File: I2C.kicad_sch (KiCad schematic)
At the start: 14 parts, among them J701 Conn_01x04, J702 Conn_01x04, U701 RCLAMP0524P-N

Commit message: Rename Ferrite_Bead to FerriteBead
Symbol name changed between KiCad 5 and 6...
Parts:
- FB701, FB702, FB703: symbol Device:Ferrite_Bead -> Device:FerriteBead
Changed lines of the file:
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@@
     (pin "1")
   )
-  (symbol (lib_id "Device:Ferrite_Bead") (at 142.24 68.58 90) (mirror x) (unit 1)
+  (symbol (lib_id "Device:FerriteBead") (at 142.24 68.58 90) (mirror x) (unit 1)
     (in_bom yes) (on_board yes)
     (property "Reference" "FB701" (id 0) (at 142.24 61.6204 90))
@@
     (pin "2")
   )
-  (symbol (lib_id "Device:Ferrite_Bead") (at 142.24 109.22 90) (mirror x) (unit 1)
+  (symbol (lib_id "Device:FerriteBead") (at 142.24 109.22 90) (mirror x) (unit 1)
     (in_bom yes) (on_board yes)
     (property "Reference" "FB703" (id 0) (at 142.24 102.2604 90))
@@
     (pin "2")
   )
-  (symbol (lib_id "Device:Ferrite_Bead") (at 142.24 88.9 90) (mirror x) (unit 1)
+  (symbol (lib_id "Device:FerriteBead") (at 142.24 88.9 90) (mirror x) (unit 1)
     (in_bom yes) (on_board yes)
     (property "Reference" "FB702" (id 0) (at 142.24 81.9404 90))

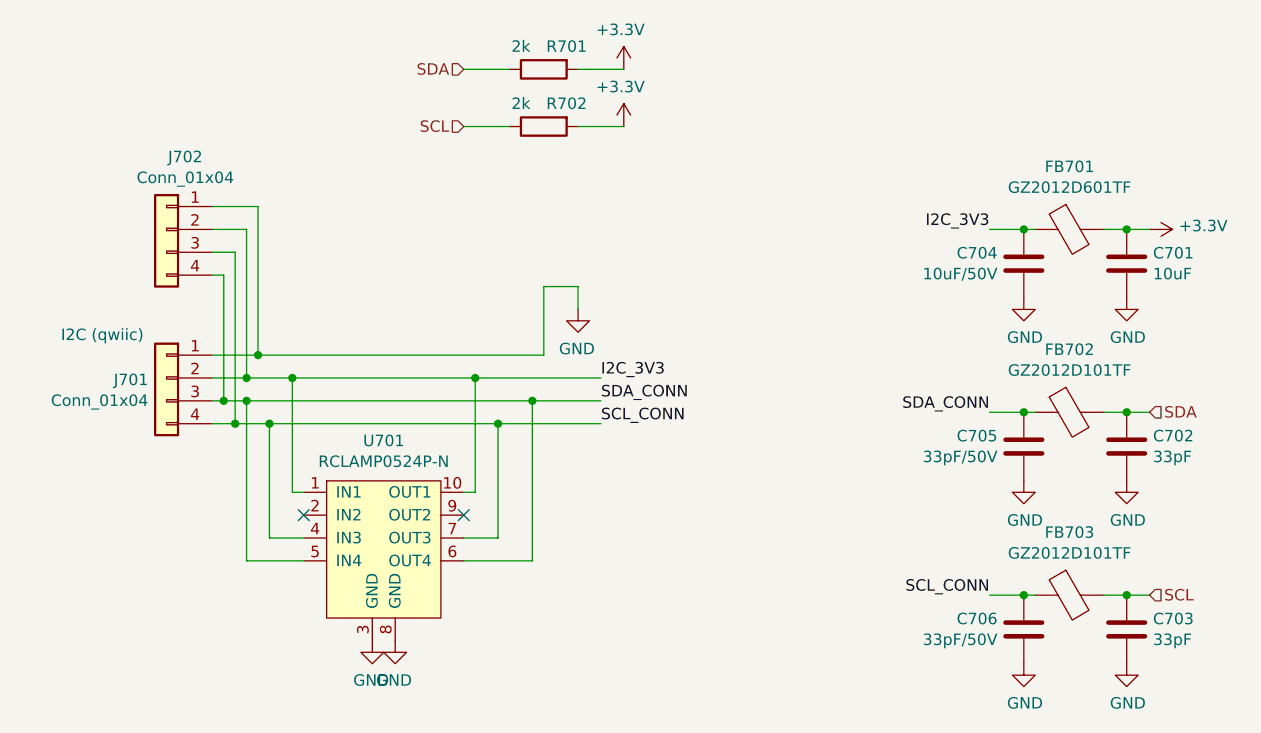
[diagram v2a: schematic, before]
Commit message: Only use the edge signal pins of RCLAMPs if possible
This improves resiliency to slight misalignment during manufacturing.
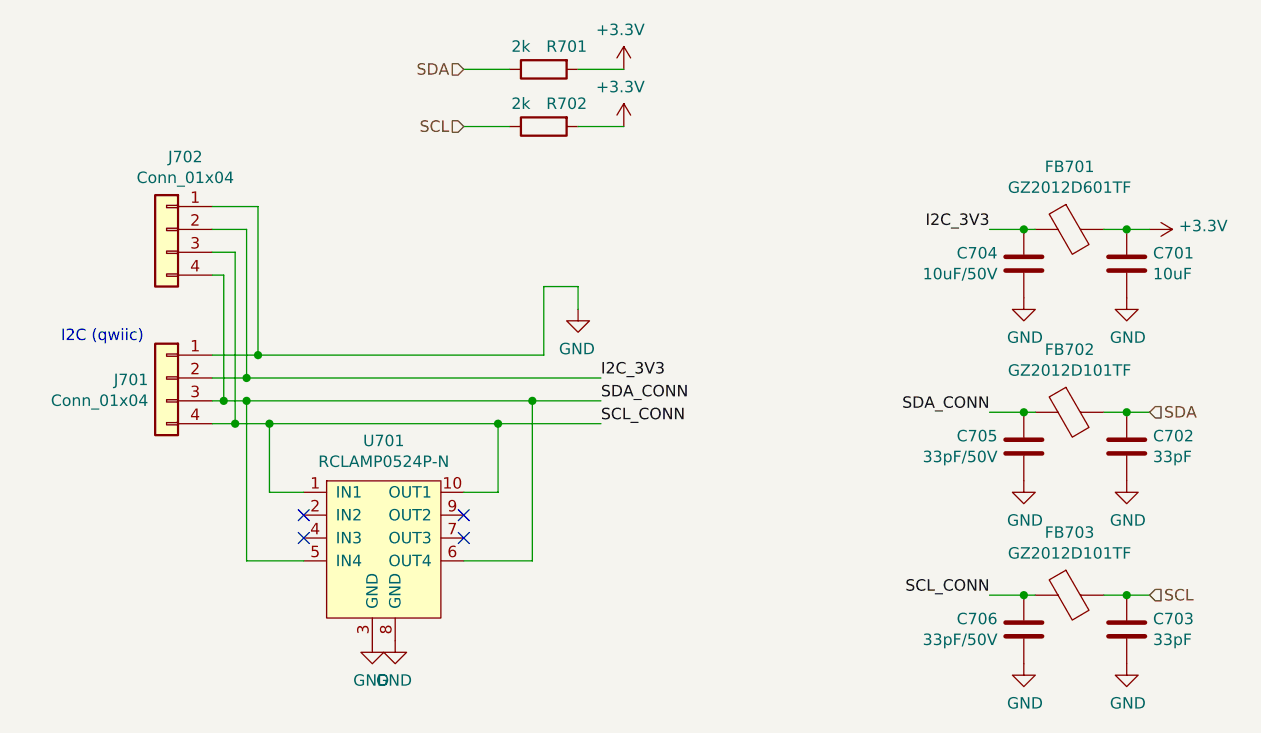
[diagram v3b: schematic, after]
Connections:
- net I2C_3V3: no longer U701.1 (IN1), U701.10 (OUT1)
- net SCL_CONN: now also U701.1 (IN1), U701.10 (OUT1); no longer U701.4 (IN3), U701.7 (OUT3)
- no-connect marks 2 -> 4
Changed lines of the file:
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@@
     (comment 3 "SH-ESP32 is licensed under CC BY-SA 4.0.")
-  )
-  (junction (at 55.88 85.09) (diameter 0) (color 0 0 0 0)
   )
   (junction (at 137.16 109.22) (diameter 0) (color 0 0 0 0)
@@
   (junction (at 50.8 87.63) (diameter 0) (color 0 0 0 0)
   )
-  (junction (at 76.2 85.09) (diameter 0) (color 0 0 0 0)
-  )
+  (no_connect (at 74.93 102.87))
   (no_connect (at 57.15 100.33))
   (no_connect (at 74.93 100.33))
+  (no_connect (at 57.15 102.87))
   (wire (pts (xy 52.07 66.04) (xy 52.07 82.55))
     (stroke (width 0) (type default) (color 0 0 0 0))
@@
   )
   (wire (pts (xy 50.8 105.41) (xy 50.8 87.63))
-    (stroke (width 0) (type default) (color 0 0 0 0))
-  )
-  (wire (pts (xy 55.88 85.09) (xy 50.8 85.09))
     (stroke (width 0) (type default) (color 0 0 0 0))
   )
@@
     (stroke (width 0) (type default) (color 0 0 0 0))
   )
-  (wire (pts (xy 55.88 97.79) (xy 55.88 85.09))
-    (stroke (width 0) (type default) (color 0 0 0 0))
-  )
   (wire (pts (xy 74.93 50.8) (xy 80.01 50.8))
     (stroke (width 0) (type default) (color 0 0 0 0))
@@
     (stroke (width 0) (type default) (color 0 0 0 0))
   )
-  (wire (pts (xy 74.93 97.79) (xy 76.2 97.79))
+  (wire (pts (xy 74.93 97.79) (xy 78.74 97.79))
     (stroke (width 0) (type default) (color 0 0 0 0))
   )
@@
     (stroke (width 0) (type default) (color 0 0 0 0))
   )
-  (wire (pts (xy 76.2 85.09) (xy 55.88 85.09))
+  (wire (pts (xy 50.8 85.09) (xy 90.17 85.09))
     (stroke (width 0) (type default) (color 0 0 0 0))
   )
@@
     (stroke (width 0) (type default) (color 0 0 0 0))
   )
-  (wire (pts (xy 76.2 97.79) (xy 76.2 85.09))
-    (stroke (width 0) (type default) (color 0 0 0 0))
-  )
   (wire (pts (xy 83.82 74.93) (xy 87.63 74.93))
     (stroke (width 0) (type default) (color 0 0 0 0))
@@
     (stroke (width 0) (type default) (color 0 0 0 0))
   )
-  (wire (pts (xy 53.34 102.87) (xy 53.34 90.17))
+  (wire (pts (xy 53.34 97.79) (xy 53.34 90.17))
     (stroke (width 0) (type default) (color 0 0 0 0))
   )
@@
     (stroke (width 0) (type default) (color 0 0 0 0))
   )
-  (wire (pts (xy 78.74 90.17) (xy 78.74 102.87))
+  (wire (pts (xy 78.74 90.17) (xy 78.74 97.79))
     (stroke (width 0) (type default) (color 0 0 0 0))
   )
   (wire (pts (xy 49.53 71.12) (xy 49.53 90.17))
-    (stroke (width 0) (type default) (color 0 0 0 0))
-  )
-  (wire (pts (xy 90.17 85.09) (xy 76.2 85.09))
     (stroke (width 0) (type default) (color 0 0 0 0))
   )
@@
     (stroke (width 0) (type default) (color 0 0 0 0))
   )
-  (wire (pts (xy 46.99 66.04) (xy 52.07 66.04))
+  (wire (pts (xy 53.34 97.79) (xy 57.15 97.79))
     (stroke (width 0) (type default) (color 0 0 0 0))
   )
-  (wire (pts (xy 57.15 102.87) (xy 53.34 102.87))
-    (stroke (width 0) (type default) (color 0 0 0 0))
-  )
-  (wire (pts (xy 57.15 97.79) (xy 55.88 97.79))
+  (wire (pts (xy 46.99 66.04) (xy 52.07 66.04))
     (stroke (width 0) (type default) (color 0 0 0 0))
   )
@@
     (stroke (width 0) (type default) (color 0 0 0 0))
   )
-  (wire (pts (xy 78.74 102.87) (xy 74.93 102.87))
-    (stroke (width 0) (type default) (color 0 0 0 0))
-  )

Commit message: Improve connector ESD protection; bump version to 2.0.2
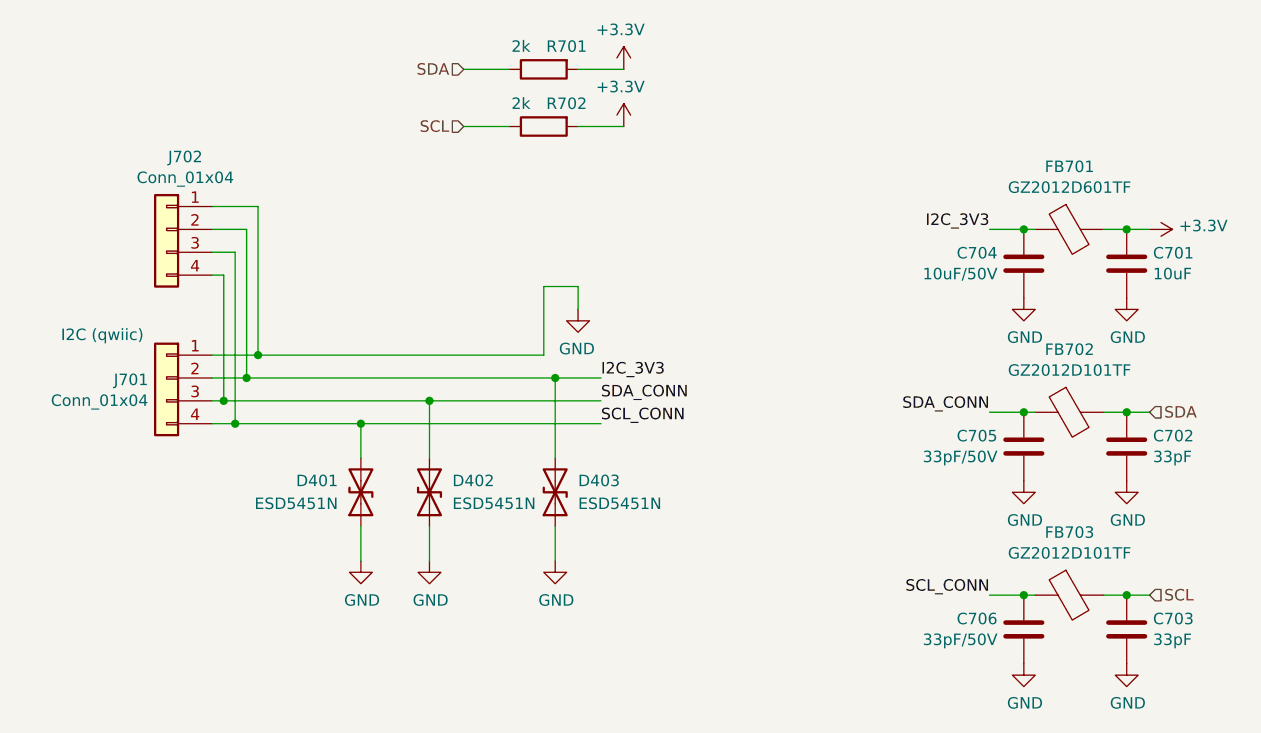
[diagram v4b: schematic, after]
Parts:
- removed U701: RCLAMP0524P-N, Package_DFN_QFN:Diodes_UDFN-10_1.0x2.5mm_P0.5mm, symbol SH-ESP32:RCLAMP0524P-N
- added D401, D402, D403: ESD5451N, Diode_SMD:D_0402_1005Metric, symbol Device:D_TVS
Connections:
- net GND: now also D401.1 (A1), D402.1 (A1), D403.1 (A1)
- net I2C_3V3: now also D403.2 (A2)
- net SCL_CONN: now also D401.2 (A2)
- net SDA_CONN: now also D402.2 (A2)
- no-connect marks 4 -> 0

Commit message: Fix component rotations
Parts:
- J701: JLCPCB_CORRECTION (none) -> 0;0;180
- J702: JLCPCB_CORRECTION (none) -> 0;3.81;90
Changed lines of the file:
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@@
       (effects (font (size 1.27 1.27)) hide)
     )
-    (property "JLCPCB_CORRECTION" "" (at 41.91 68.58 0)
+    (property "JLCPCB_CORRECTION" "0;3.81;90" (at 41.91 68.58 0)
       (effects (font (size 1.27 1.27)) hide)
     )
@@
       (effects (font (size 1.27 1.27)) hide)
     )
-    (property "JLCPCB_CORRECTION" "" (at 41.91 85.09 0)
+    (property "JLCPCB_CORRECTION" "0;0;180" (at 41.91 85.09 0)
       (effects (font (size 1.27 1.27)) hide)
     )

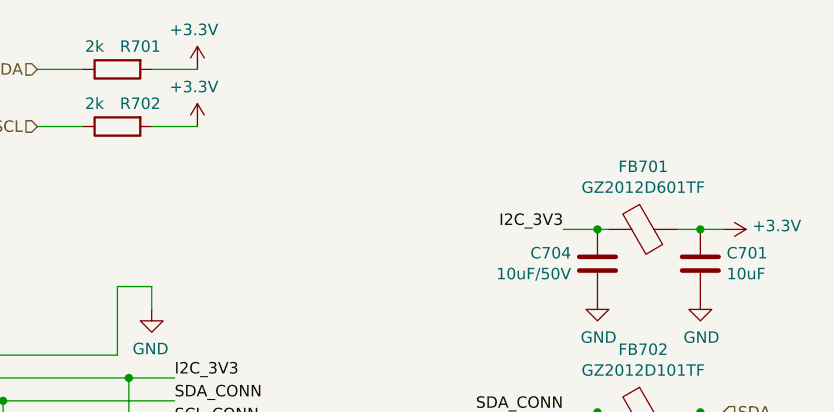
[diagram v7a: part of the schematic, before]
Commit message: Go back to ISO1050 for CAN transceiver
Also add CAN RX and TX LEDs and beef up buck capacitors
as much as space allows.
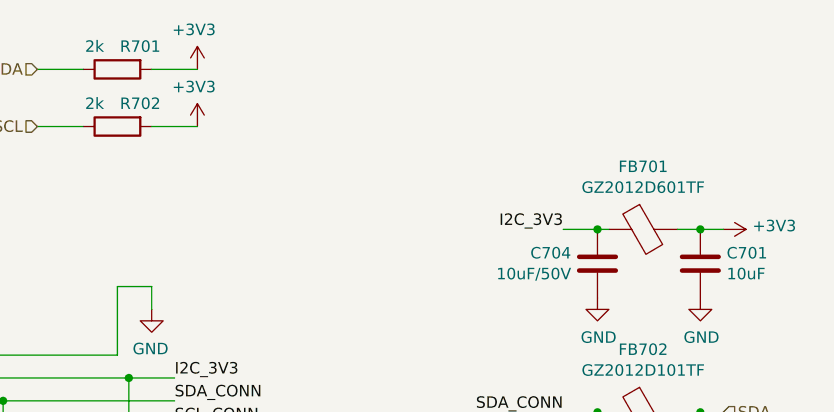
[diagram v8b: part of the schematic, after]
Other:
- company: Hat Labs Ltd -> Hat Labs Oy
- title: Sailor Hat with ESP32 -> SH-ESP32
